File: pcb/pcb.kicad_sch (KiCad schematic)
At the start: 61 parts, among them J1 USB_C_Receptacle_USB2.0, J2 Conn_01x05, SW1 SW_Push, SW2 SW_Push, U1 XC6206P332MR, U2 SRV05-4, U3 DRV5056A3xDBZxQ1, U4 DRV5056A3xDBZxQ1, U5 DRV5056A3xDBZxQ1, U6 RP2040, U7 W25Q128JVS, Y1 12MHz

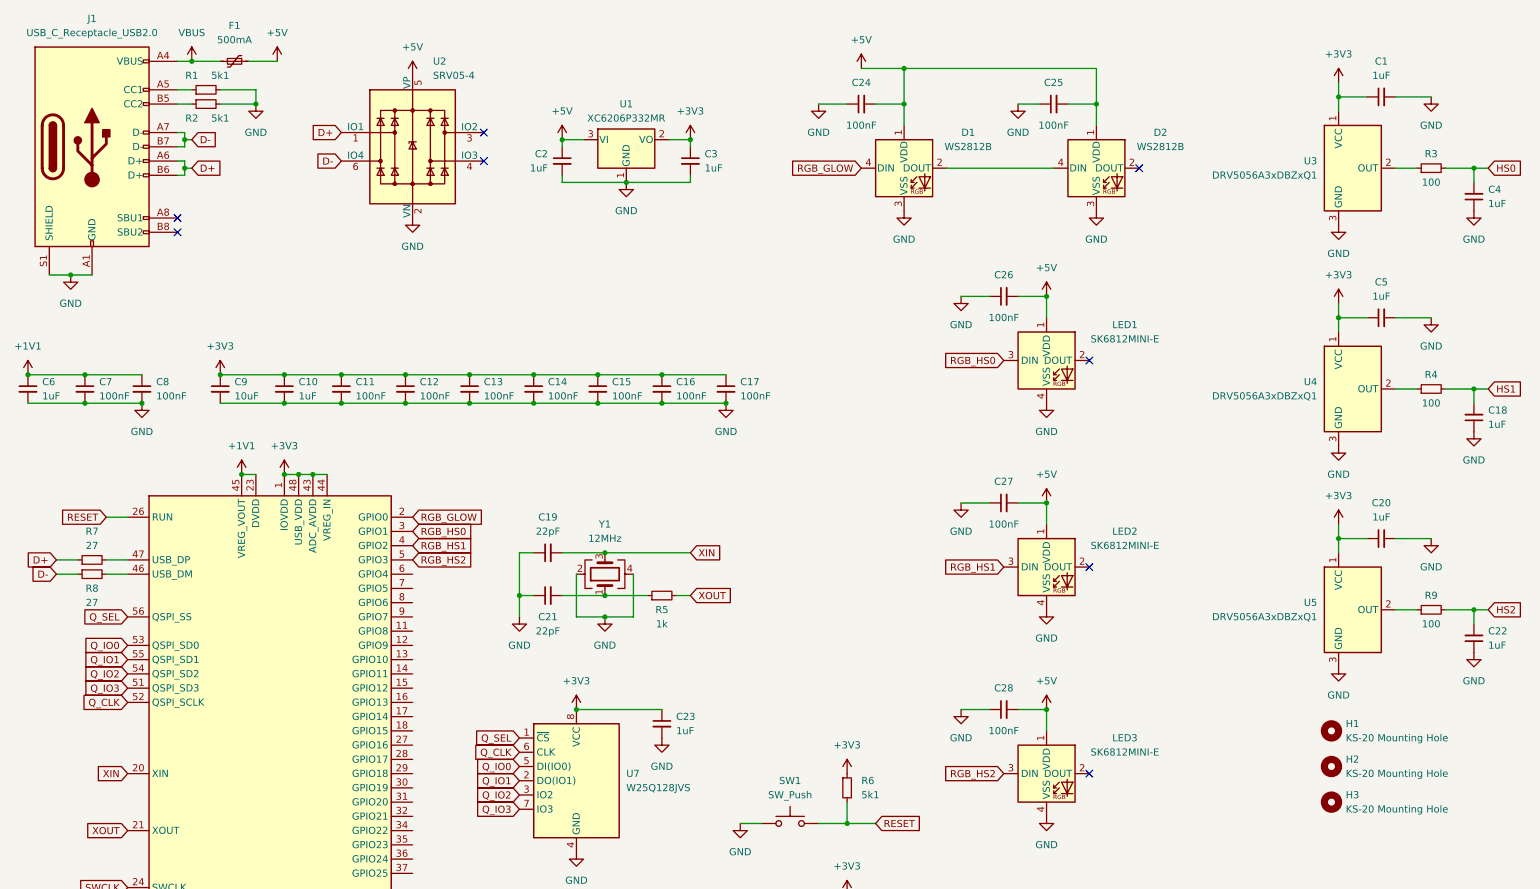
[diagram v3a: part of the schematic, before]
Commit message: feat: initial attempt at laying out pcb
routing will be tricky - might need a 4 layer pcb due to the mixed voltages...

probably better to remove the in-switch LEDs for the time being...
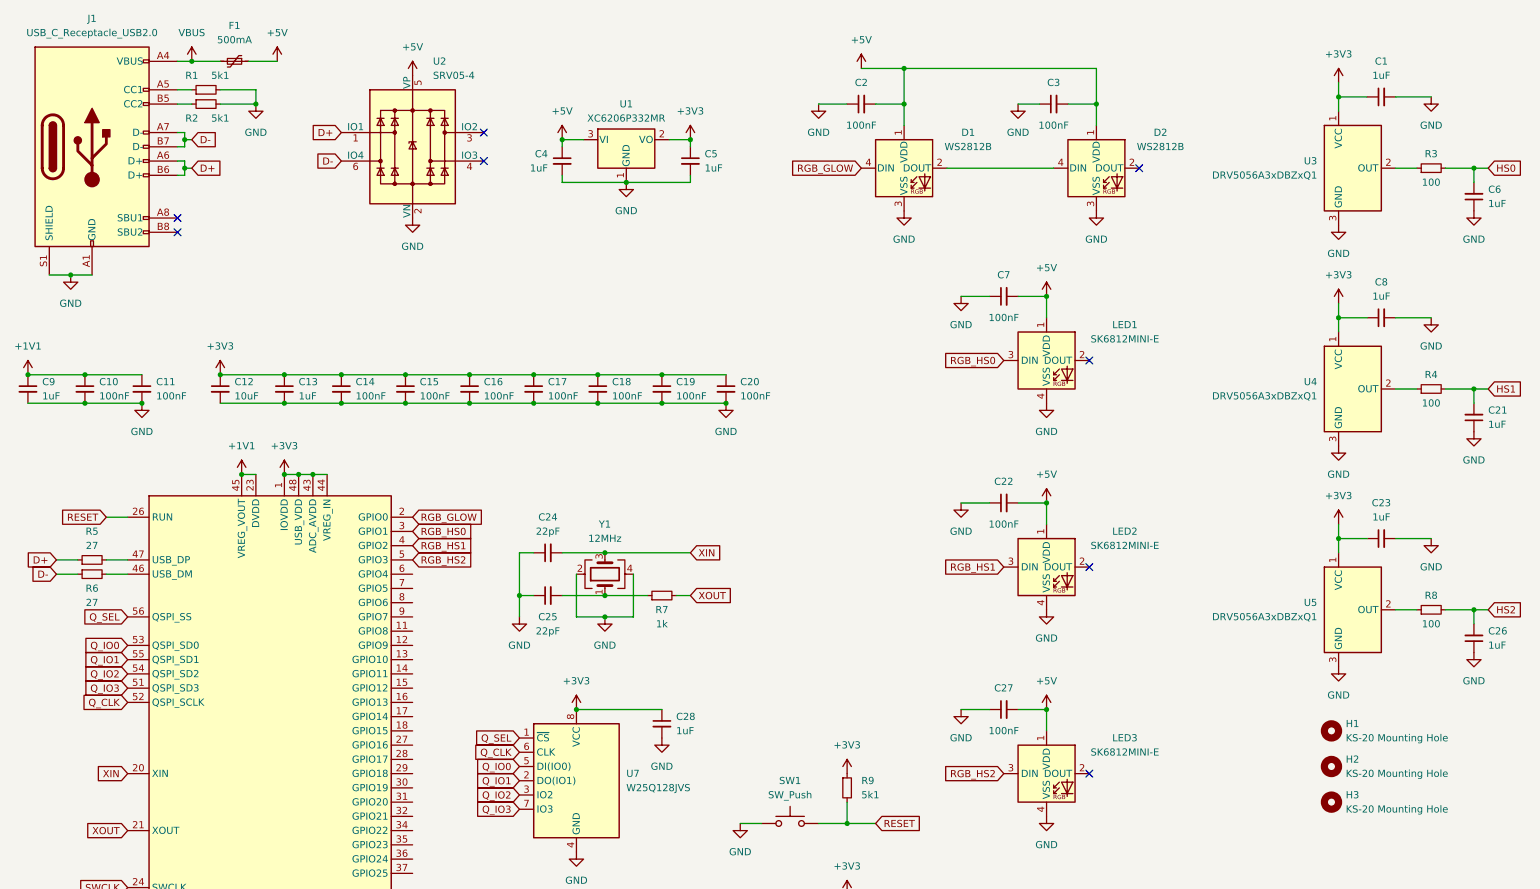
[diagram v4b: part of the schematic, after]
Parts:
- renumbered C7 to C10, C8 to C11, C9 to C12, C10 to C13, C11 to C14, C12 to C15, C13 to C16, C14 to C17, C15 to C18, C16 to C19, C24 to C2, C17 to C20, C18 to C21, C27 to C22, C20 to C23, C19 to C24, C21 to C25, C22 to C26, C28 to C27, C23 to C28, C25 to C3, C2 to C4, C3 to C5, C4 to C6, C26 to C7, C5 to C8, C6 to C9, R7 to R5, R8 to R6, R5 to R7, R9 to R8, R6 to R9

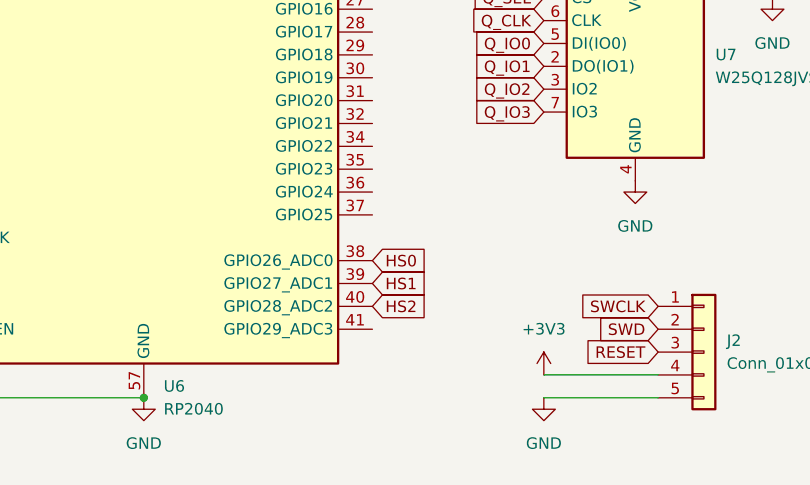
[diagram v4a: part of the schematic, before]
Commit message: feat: initial attempt at placing and routing key components
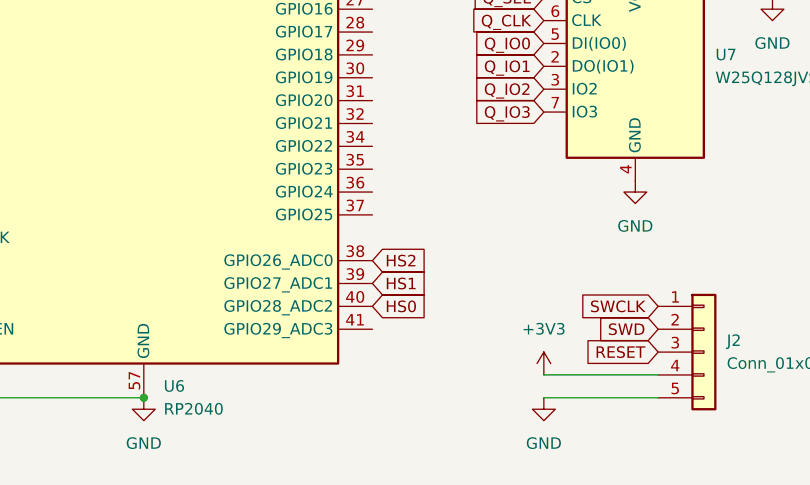
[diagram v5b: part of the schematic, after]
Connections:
- net HS0: now also U6.40 (GPIO28_ADC2); no longer U6.38 (GPIO26_ADC0)
- net HS2: now also U6.38 (GPIO26_ADC0); no longer U6.40 (GPIO28_ADC2)
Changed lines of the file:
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@@
     )
   )
-  (global_label "HS2" (shape input) (at 85.09 177.8 0) (fields_autoplaced)
+  (global_label "HS2" (shape input) (at 85.09 172.72 0) (fields_autoplaced)
+    (effects (font (size 1.27 1.27)) (justify left))
+    (property "Intersheetrefs" "${INTERSHEET_REFS}" (at 91.8247 172.72 0)
+      (effects (font (size 1.27 1.27)) (justify left) hide)
+    )
+  )
+  (global_label "HS0" (shape input) (at 85.09 177.8 0) (fields_autoplaced)
     (effects (font (size 1.27 1.27)) (justify left))
     (property "Intersheetrefs" "${INTERSHEET_REFS}" (at 91.8247 177.8 0)
       (effects (font (size 1.27 1.27)) (justify left) hide)
     )
-  )
-  (global_label "HS0" (shape input) (at 85.09 172.72 0) (fields_autoplaced)
-    (effects (font (size 1.27 1.27)) (justify left))
-    (property "Intersheetrefs" "${INTERSHEET_REFS}" (at 91.8247 172.72 0)
-      (effects (font (size 1.27 1.27)) (justify left) hide)
-    )

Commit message: fix: add 3.3v to 5v logic conversion
this uses the 74AHCT1G125. there are values that can step up multiple pins at once, but it seems cheaper to just use individual ones. it should also be easier to route, as the logic level conversion can be placed next to each relevant location.
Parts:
- removed C22, C27: 100nF, Capacitor_SMD:C_0402_1005Metric, symbol Device:C_Small
- added C10, C11: 100nF, Capacitor_SMD:C_0402_1005Metric, symbol Device:C_Small
- added R10, R6, R7, R8: 1k, Resistor_SMD:R_0402_1005Metric, symbol Device:R_Small
- added U6, U7, U8, U9: 74AHCT1G125, Package_TO_SOT_SMD:SOT-353_SC-70-5, symbol 74xGxx:74AHCT1G125
- renumbered C9 to C12, C10 to C13, C11 to C14, C12 to C15, C13 to C16, C14 to C17, C15 to C18, C16 to C19, C8 to C2, C17 to C20, C18 to C21, C19 to C22, C20 to C23, C2 to C26, C3 to C27, C23 to C3, C21 to C7, C26 to C8, C7 to C9, R5 to R11, R10 to R12, R6 to R13, R9 to R14, R11 to R15, R12 to R16, R8 to R5, R7 to R9, U2 to U1, U6 to U10, U7 to U11, U1 to U2
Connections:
- net +5V: now also C10.2, C11.2, U6.5 (VCC), U7.5 (VCC), U8.5 (VCC), U9.5 (VCC)
- net GND: now also C10.1, C11.1, R10.2, R6.2, R7.2, R8.2, U6.3 (GND), U7.3 (GND), U8.3 (GND), U9.3 (GND)
- net RGB_GLOW: now also U9.2; no longer D1.4 (DIN)
- net RGB_HS0: now also U6.2; no longer LED1.3 (DIN)
- net RGB_HS1: now also U7.2; no longer LED2.3 (DIN)
- net RGB_HS2: now also U8.2; no longer LED3.3 (DIN)
- new net: R6.1, U6.1
- new net: LED1.3 (DIN), U6.4
- new net: R10.1, U9.1
- new net: R8.1, U8.1
- new net: LED3.3 (DIN), U8.4
- new net: R7.1, U7.1
- new net: D1.4 (DIN), U9.4
- new net: LED2.3 (DIN), U7.4
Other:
- note added: "Boot Select"
- note added: "Crystal"
- note added: "Debug Header"
- note added: "Decoupling Capacitors"
- note added: "Flash Memory"
- note added: "Hall Sensors"
- note added: "Keyswitch RGB LEDs"
- note added: "LDO Voltage Regulator"
- note added: "Mounting Holes"
- note added: "RP2040 MCU"
- note added: "Reset Switch"
- note added: "USB Type-C Receptacle"
- note added: "Underglow RGB LEDs"
- moved on the sheet: C1, C12, C13, C14, C15, C16, C17, C18, C19, C2, C20, C21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

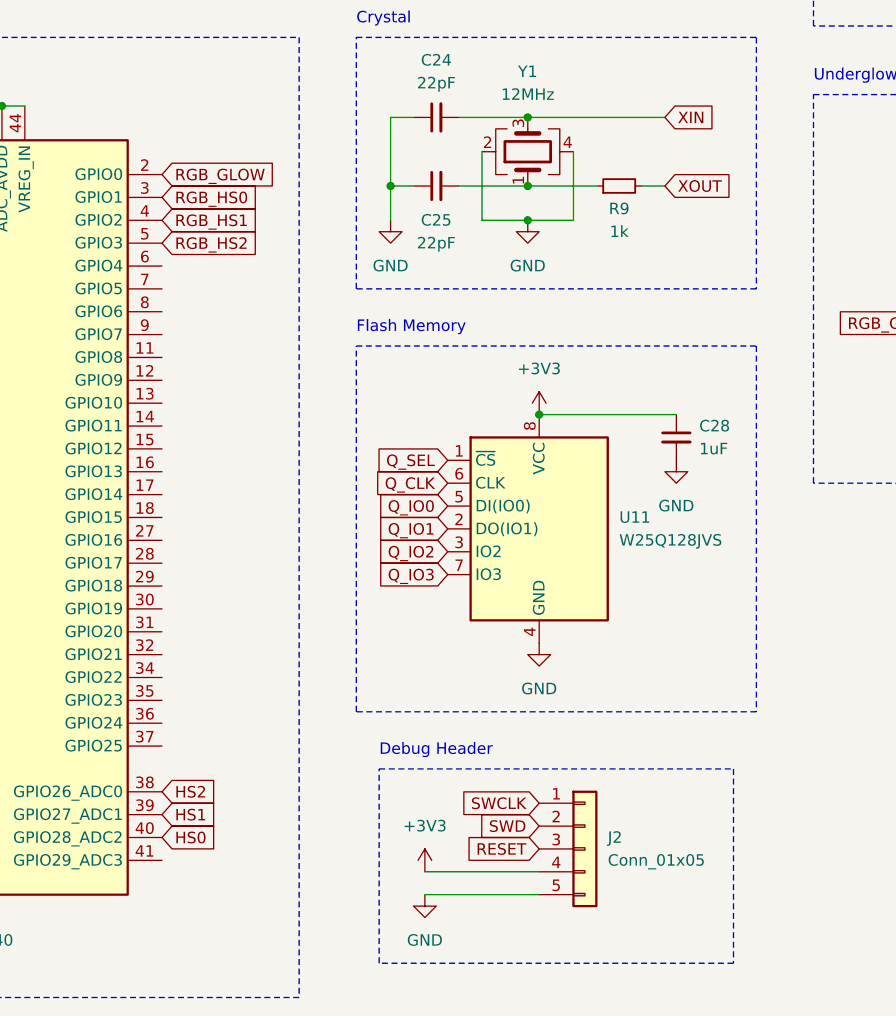
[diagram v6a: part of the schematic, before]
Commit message: feat: fully connected pcb
ended up removing the debug header - I don't think these appear in production boards anyway, so should be OK.

there's probably a better way to route the analog lines, but I couldn't come up with anything for it...
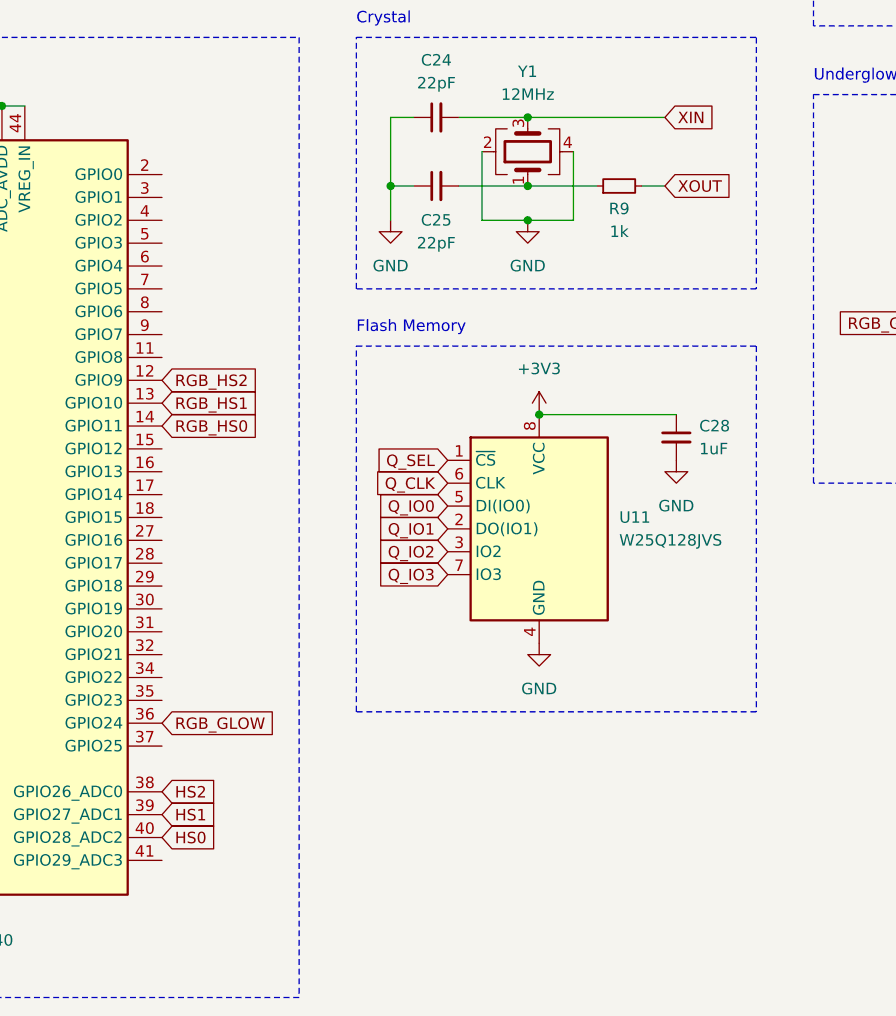
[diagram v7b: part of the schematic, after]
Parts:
- removed J2: Conn_01x05, Connector_PinHeader_2.54mm:PinHeader_1x05_P2.54mm_Horizontal, symbol Connector_Generic:Conn_01x05
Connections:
- net RGB_GLOW: now also U10.36 (GPIO24); no longer U10.2 (GPIO0)
- net RGB_HS0: now also U10.14 (GPIO11); no longer U10.3 (GPIO1)
- net RGB_HS1: now also U10.13 (GPIO10); no longer U10.4 (GPIO2)
- net RGB_HS2: now also U10.12 (GPIO9); no longer U10.5 (GPIO3)
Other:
- note removed: "Debug Header"
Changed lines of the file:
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@@
     (stroke (width 0) (type default))
   )
-  (wire (pts (xy 118.11 205.74) (xy 130.81 205.74))
-    (stroke (width 0) (type default))
-  )
   (wire (pts (xy 129.54 119.38) (xy 144.78 119.38))
     (stroke (width 0) (type default))
@@
     (stroke (width 0) (type default))
   )
-  (wire (pts (xy 118.11 203.2) (xy 130.81 203.2))
-    (stroke (width 0) (type default))
-  )
   (wire (pts (xy 218.44 130.81) (xy 223.52 130.81))
     (stroke (width 0) (type default))
@@
     (fill (type none))
   )
-  (rectangle (start 113.03 191.77) (end 152.4 213.36)
-    (stroke (width 0) (type dash))
-    (fill (type none))
-  )
   (text "Decoupling Capacitors" (at 16.51 80.01 0)
     (effects (font (size 1.27 1.27)) (justify left bottom))
@@
     (effects (font (size 1.27 1.27)) (justify left bottom))
   )
-  (text "Debug Header" (at 113.03 190.5 0)
-    (effects (font (size 1.27 1.27)) (justify left bottom))
-  )
   (text "Mounting Holes" (at 175.26 167.64 0)
     (effects (font (size 1.27 1.27)) (justify left bottom))
@@
     )
   )
-  (global_label "RGB_HS2" (shape input) (at 88.9 133.35 0) (fields_autoplaced)
+  (global_label "RGB_HS2" (shape input) (at 88.9 148.59 0) (fields_autoplaced)
     (effects (font (size 1.27 1.27)) (justify left))
-    (property "Intersheetrefs" "${INTERSHEET_REFS}" (at 100.4123 133.35 0)
+    (property "Intersheetrefs" "${INTERSHEET_REFS}" (at 100.4123 148.59 0)
       (effects (font (size 1.27 1.27)) (justify left) hide)
     )
@@
     )
   )
-  (global_label "SWCLK" (shape input) (at 130.81 195.58 180) (fields_autoplaced)
-    (effects (font (size 1.27 1.27)) (justify right))
-    (property "Intersheetrefs" "${INTERSHEET_REFS}" (at 121.5958 195.58 0)
-      (effects (font (size 1.27 1.27)) (justify right) hide)
-    )
-  )
   (global_label "Q_IO2" (shape input) (at 38.1 153.67 180) (fields_autoplaced)
     (effects (font (size 1.27 1.27)) (justify right))
@@
     )
   )
-  (global_label "RGB_HS1" (shape input) (at 88.9 130.81 0) (fields_autoplaced)
+  (global_label "RGB_HS1" (shape input) (at 88.9 151.13 0) (fields_autoplaced)
     (effects (font (size 1.27 1.27)) (justify left))
-    (property "Intersheetrefs" "${INTERSHEET_REFS}" (at 100.4123 130.81 0)
+    (property "Intersheetrefs" "${INTERSHEET_REFS}" (at 100.4123 151.13 0)
       (effects (font (size 1.27 1.27)) (justify left) hide)
     )
@@
     )
   )
-  (global_label "RGB_HS0" (shape input) (at 88.9 128.27 0) (fields_autoplaced)
+  (global_label "RGB_HS0" (shape input) (at 88.9 153.67 0) (fields_autoplaced)
     (effects (font (size 1.27 1.27)) (justify left))
-    (property "Intersheetrefs" "${INTERSHEET_REFS}" (at 100.4123 128.27 0)
+    (property "Intersheetrefs" "${INTERSHEET_REFS}" (at 100.4123 153.67 0)
       (effects (font (size 1.27 1.27)) (justify left) hide)
     )
@@
     )
   )
-  (global_label "SWD" (shape input) (at 130.81 198.12 180) (fields_autoplaced)
-    (effects (font (size 1.27 1.27)) (justify right))
-    (property "Intersheetrefs" "${INTERSHEET_REFS}" (at 123.8939 198.12 0)
-      (effects (font (size 1.27 1.27)) (justify right) hide)
-    )
-  )
   (global_label "HS1" (shape input) (at 306.07 44.45 0) (fields_autoplaced)
     (effects (font (size 1.27 1.27)) (justify left))
@@
     )
   )
-  (global_label "RESET" (shape input) (at 130.81 200.66 180) (fields_autoplaced)
-    (effects (font (size 1.27 1.27)) (justify right))
-    (property "Intersheetrefs" "${INTERSHEET_REFS}" (at 122.0797 200.66 0)
-      (effects (font (size 1.27 1.27)) (justify right) hide)
-    )
-  )
   (global_label "Q_CLK" (shape input) (at 38.1 158.75 180) (fields_autoplaced)
     (effects (font (size 1.27 1.27)) (justify right))
@@
     )
   )
-  (global_label "RGB_GLOW" (shape input) (at 88.9 125.73 0) (fields_autoplaced)
+  (global_label "RGB_GLOW" (shape input) (at 88.9 186.69 0) (fields_autoplaced)
     (effects (font (size 1.27 1.27)) (justify left))
-    (property "Intersheetrefs" "${INTERSHEET_REFS}" (at 101.7428 125.73 0)
+    (property "Intersheetrefs" "${INTERSHEET_REFS}" (at 101.7428 186.69 0)
       (effects (font (size 1.27 1.27)) (justify left) hide)
     )
@@
     )
   )
-  (symbol (lib_id "power:+3V3") (at 118.11 203.2 0) (unit 1)
-    (in_bom yes) (on_board yes) (dnp no) (fields_autoplaced)
-    (property "Reference" "#PWR063" (at 118.11 207.01 0)
-      (effects (font (size 1.27 1.27)) hide)
-    )
-    (property "Value" "+3V3" (at 118.11 198.12 0)
-      (effects (font (size 1.27 1.27)))
-    )
-    (property "Footprint" "" (at 118.11 203.2 0)
-      (effects (font (size 1.27 1.27)) hide)
-    )
-    (property "Datasheet" "" (at 118.11 203.2 0)
-      (effects (font (size 1.27 1.27)) hide)
-    )
-    (pin "1")
-    (instances
-      (project "pcb"
-        (path "/fe0c1c23-b294-4653-a8db-85682224ef67"
-          (reference "#PWR063") (unit 1)
-        )
-      )
-    )
-  )
   (symbol (lib_id "Device:C_Small") (at 76.2 91.44 0) (unit 1)
     (in_bom yes) (on_board yes) (dnp no) (fields_autoplaced)
@@
     )
   )
-  (symbol (lib_id "Connector_Generic:Conn_01x05") (at 135.89 200.66 0) (unit 1)
-    (in_bom yes) (on_board yes) (dnp no) (fields_autoplaced)
-    (property "Reference" "J2" (at 138.43 199.39 0)
-      (effects (font (size 1.27 1.27)) (justify left))
-    )
-    (property "Value" "Conn_01x05" (at 138.43 201.93 0)
-      (effects (font (size 1.27 1.27)) (justify left))
-    )
-    (property "Footprint" "Connector_PinHeader_2.54mm:PinHeader_1x05_P2.54mm_Horizontal" (at 135.89 200.66 0)
-      (effects (font (size 1.27 1.27)) hide)
-    )
-    (property "Datasheet" "~" (at 135.89 200.66 0)
-      (effects (font (size 1.27 1.27)) hide)
-    )
-    (pin "1")
-    (pin "2")
-    (pin "3")
-    (pin "4")
-    (pin "5")
-    (instances
-      (project "pcb"
-        (path "/fe0c1c23-b294-4653-a8db-85682224ef67"
-          (reference "J2") (unit 1)
-        )
-      )
-    )
-  )
   (symbol (lib_id "Device:C_Small") (at 245.11 49.53 180) (unit 1)
     (in_bom yes) (on_board yes) (dnp no) (fields_autoplaced)
@@
         )
       )
-    )
-  )
-  (symbol (lib_id "power:GND") (at 118.11 205.74 0) (unit 1)
-    (in_bom yes) (on_board yes) (dnp no) (fields_autoplaced)
-    (property "Reference" "#PWR064" (at 118.11 212.09 0)
-      (effects (font (size 1.27 1.27)) hide)
-    )
-    (property "Value" "GND" (at 118.11 210.82 0)
-      (effects (font (size 1.27 1.27)))
-    )
-    (property "Footprint" "" (at 118.11 205.74 0)
-      (effects (font (size 1.27 1.27)) hide)
-    )
-    (property "Datasheet" "" (at 118.11 205.74 0)
-      (effects (font (size 1.27 1.27)) hide)
-    )
-    (pin "1")
-    (instances
-      (project "pcb"
-        (path "/fe0c1c23-b294-4653-a8db-85682224ef67"
-          (reference "#PWR064") (unit 1)
-        )
-      )
